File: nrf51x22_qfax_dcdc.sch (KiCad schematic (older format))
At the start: 22 parts, among them U1 nrf51822-qfax, X1 Crystal-4, X2 32.768kHz

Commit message: schematic and netlist imported to board
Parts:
- removed C12: 1.0uF, dcdc:CAPC1608X06L, symbol C
- removed C5: 3.9pF, dcdc:CAPC1005X04L, symbol C
- removed C9: 1.0nF, dcdc:CAPC1005X04L, symbol C
- removed L1: 4.7nH, dcdc:INDC1005X04L, symbol L_Small
- removed L2: 27nH, dcdc:INDC1005X04L, symbol L_Small
- added C7: 100pF, dcdc:CAPC1005X04L, symbol C
- C10: value 47nF -> 1.0uF; footprint dcdc:CAPC1005X04L -> dcdc:CAPC1608X06L; Distributor 1 311-1717-1-ND -> .; Manufacturer Yageo -> .; Manufacturer Part CC0402KRX7R8BB473 -> .
- C3: value 2.2nF -> .8pF; Description Capacitor X7R ±10% -> Capacitor NP0 ±5%; Distributor 1 311-1037-1-ND -> .; Manufacturer Yageo -> .; Manufacturer Part CC0402KRX7R9BB222 -> .
- C4: value 1.0pF -> 100nF; Description Capacitor NP0 ±0.1pF -> Capacitor X7R ±10%; Distributor 1 (none) -> .; Manufacturer (none) -> .; Manufacturer Part (none) -> .
- C6: value 1.5pF -> NC; footprint dcdc:CAPC1005X04L -> (none); Description Capacitor NP0 ±0.1pF -> .; Distributor 1 (none) -> .; Manufacturer (none) -> .; Manufacturer Part (none) -> .
- C8: Distributor 1 311-1345-1-ND -> (none); Distrubutor 1 (none) -> 311-1345-1-ND
- L1: renamed from L3; value 3.3nH -> 3.9nH
- U1: symbol nrf51822-qfax -> nrf52832-qfax
- X1: footprint dcdc:BT-XTAL_2520 -> (none); Description 8pF ±40ppm -> 32Mhz 8pF ±40ppm; Distributor 1 644-1169-1-ND -> .; Manufacturer NDK -> .; Manufacturer Part NX2520SA-16MHZ-STD-CSW-5 -> .
- X2: Description 9pF ±20ppm -> 32.768kHz 9pF ±20ppm
- renumbered C14 to C11, C13 to C12, C11 to C5, C7 to C9, L4 to L2, L5 to L3
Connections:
- net labels added: RF, VDD_nRF
- net labels removed: AVDD, VCC_nRF
- wire segments 57 -> 41
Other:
- moved on the sheet: C11, C12, C3, C5, C9, L1, X2

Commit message: add missing x1
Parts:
- X1: footprint (none) -> dcdc:BT-XTAL_2016
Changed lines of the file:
@@
 LIBS:valves
 LIBS:nrf51822
-LIBS:nrf51x22_qfax_dcdc-cache
 EELAYER 25 0
 EELAYER END
@@
 F 0 "X1" H 1600 5950 50  0000 C CNN
 F 1 "Crystal-4" H 1600 5450 50  0000 C CNN
-F 2 "" H 1600 5700 50  0001 C CNN
+F 2 "dcdc:BT-XTAL_2016" H 1600 5700 50  0001 C CNN
 F 3 "" H 1600 5700 50  0000 C CNN
 F 4 "32Mhz 8pF ±40ppm" H 1600 5700 60  0001 C CNN "Description"

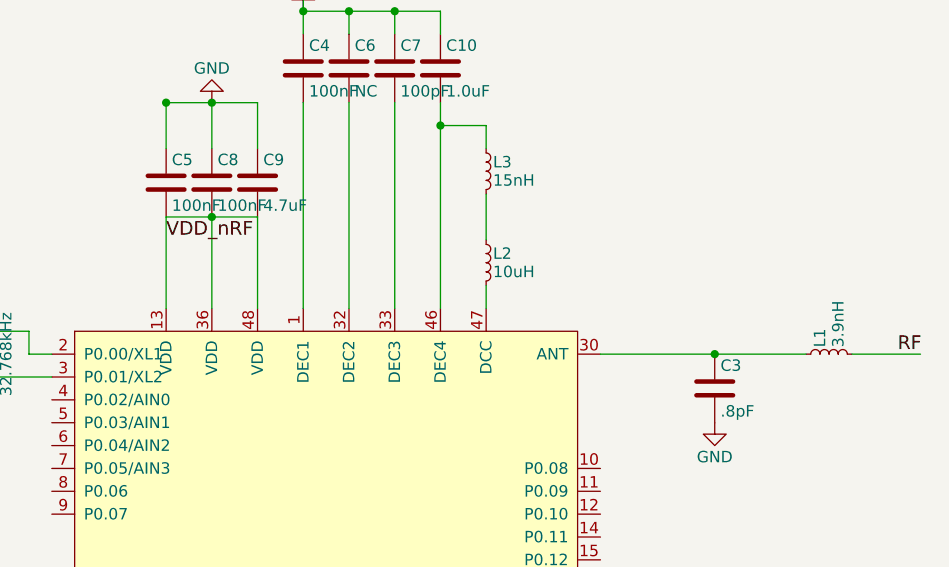
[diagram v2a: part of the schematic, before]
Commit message: swap 3 via back to vdd, and rotate parts so nets are correct
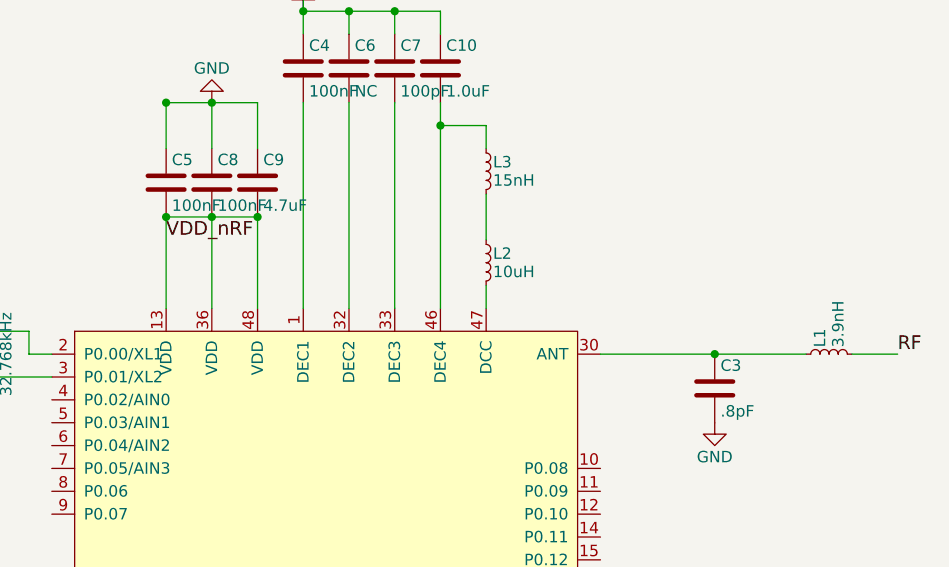
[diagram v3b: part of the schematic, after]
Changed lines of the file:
@@
 Wire Wire Line
 	900  5500 900  5900
-Wire Wire Line
-	2300 2200 2300 2600
-Wire Wire Line
-	2500 2200 2500 2600
 Connection ~ 4700 2800
 Connection ~ 2300 1700
@@
 Connection ~ 3100 1300
 Wire Wire Line
-	2700 2200 2700 2600
-Wire Wire Line
 	2700 1700 2700 1900
 Wire Wire Line
@@
 Wire Wire Line
 	2300 1900 2300 1700
-Wire Wire Line
-	5300 2800 5600 2800
 Text Label 5500 2800 0    60   ~ 0
 RF
-Wire Wire Line
-	2300 2200 2700 2200
 Connection ~ 2500 2200
 Text Label 2300 2300 0    60   ~ 0
 VDD_nRF
+Connection ~ 2300 2200
+Connection ~ 2700 2200
+Wire Wire Line
+	5300 2800 5500 2800
+Wire Wire Line
+	2500 2600 2500 2200
+Wire Wire Line
+	2300 2600 2300 2200
+Wire Wire Line
+	2700 2200 2700 2600
+Wire Wire Line
+	2300 2200 2700 2200
 $EndSCHEMATC
